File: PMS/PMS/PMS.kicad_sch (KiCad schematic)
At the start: 35 parts, among them IC1 TMCS1107A1BQDRQ1, J1 XT60PW-M, J2 XT60PW-F, J3 XT60PW-M, J4 XT60PW-F, J5 XT60PW-F, J6 Conn_01x03_Male, J7 Conn_01x02_Male, U1 ADC101C027CIMK, U2 ADC101C027CIMK, U4 REF195

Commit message: changed solder jumper footprint and added silk labels for XT60 connectors
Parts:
- JP1: footprint Jumper:SolderJumper-2_P1.3mm_Bridged2Bar_Pad1.0x1.5mm -> Jumper:SolderJumper-2_P1.3mm_Bridged2Bar_RoundedPad1.0x1.5mm
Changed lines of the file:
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@@
     (property "Reference" "JP1" (id 0) (at 88.9 58.0095 0))
     (property "Value" "Jumper_2_Bridged" (id 1) (at 88.9 60.7846 0))
-    (property "Footprint" "Jumper:SolderJumper-2_P1.3mm_Bridged2Bar_Pad1.0x1.5mm" (id 2) (at 88.9 62.611 0)
+    (property "Footprint" "Jumper:SolderJumper-2_P1.3mm_Bridged2Bar_RoundedPad1.0x1.5mm" (id 2) (at 88.9 62.611 0)
       (effects (font (size 1.27 1.27)) hide)
     )
@@
     )
     (path "/cf54f418-c583-4eda-be64-e2658e9d7854"
-      (reference "JP1") (unit 1) (value "Jumper_2_Bridged") (footprint "Jumper:SolderJumper-2_P1.3mm_Bridged2Bar_Pad1.0x1.5mm")
+      (reference "JP1") (unit 1) (value "Jumper_2_Bridged") (footprint "Jumper:SolderJumper-2_P1.3mm_Bridged2Bar_RoundedPad1.0x1.5mm")
     )
     (path "/45100c78-fff6-4f44-a47d-2aea8091517a"

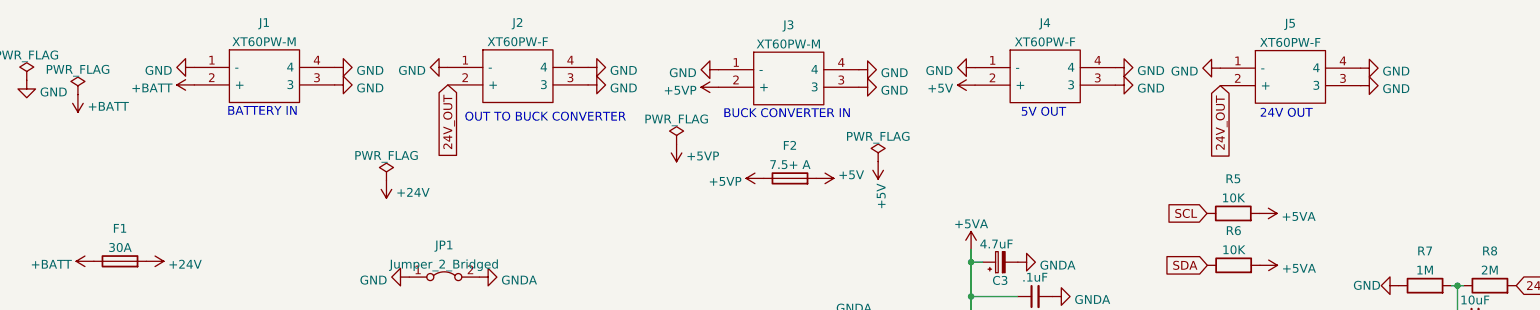
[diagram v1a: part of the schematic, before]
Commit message: changed to XT90s for 24V
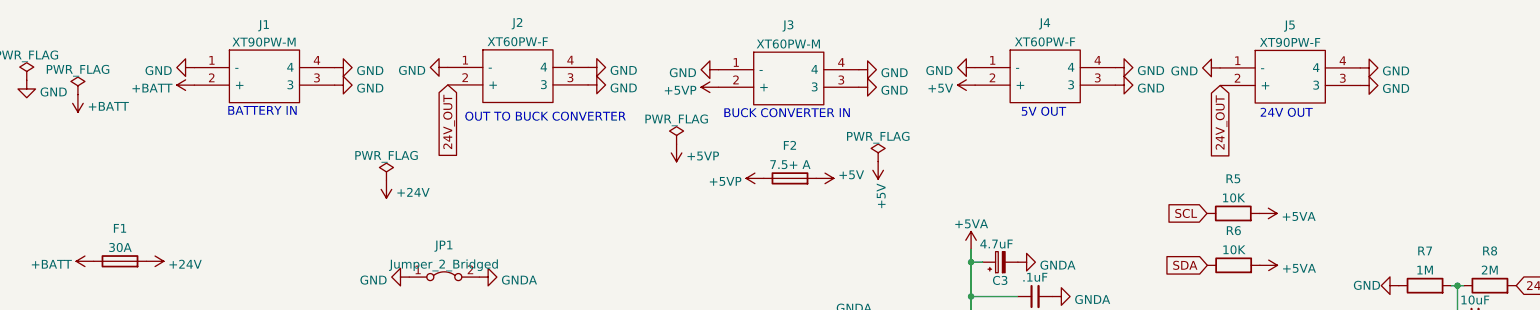
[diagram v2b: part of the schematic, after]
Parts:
- removed J1: XT60PW-M, LIB_XT60PW-M:XT60PWM, symbol XT60PW-M:XT60PW-M
- removed J5: XT60PW-F, LIB_XT60PW-F:XT60PWF, symbol XT60PW-F:XT60PW-F
- added J1: XT90PW-M, XT90PW-M:XT90PWM, symbol XT90PW-M:XT90PW-M
- added J5: XT90PW-F, XT90PW-F:XT90PW-F, symbol XT90PW-F:XT90PW-F
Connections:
- net +BATT: now also J1.2 (+)
- net 24V_OUT: now also J5.2 (+)
- net GND: now also J1.1 (-), J1.3, J1.4, J5.1 (-), J5.3, J5.4

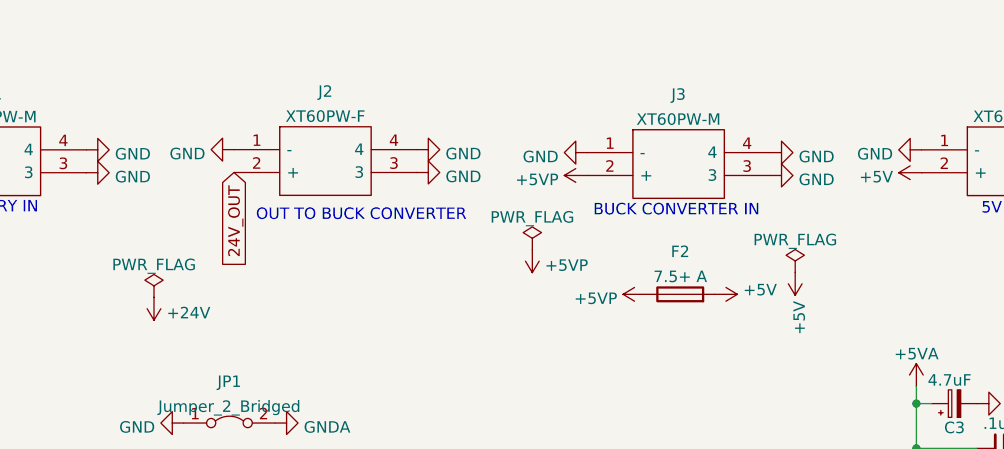
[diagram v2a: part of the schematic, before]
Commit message: Changed to barrier strip for connection to Mean-Well. Interconnects cannot be erroneously connected
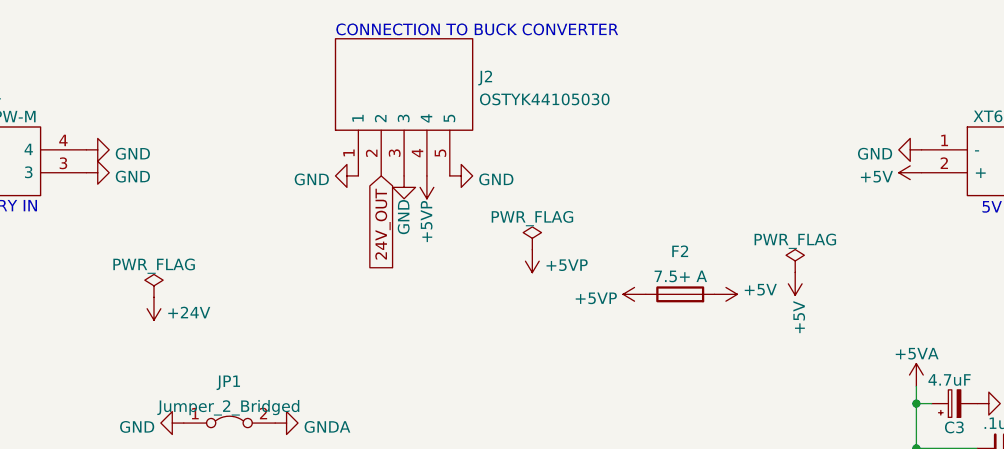
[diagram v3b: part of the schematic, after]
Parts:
- removed J2: XT60PW-F, LIB_XT60PW-F:XT60PWF, symbol XT60PW-F:XT60PW-F
- removed J3: XT60PW-M, LIB_XT60PW-M:XT60PWM, symbol XT60PW-M:XT60PW-M
- added J2: OSTYK44105030, LIB_OSTYK44105030:OSTYK44105030, symbol OSTYK44105030:OSTYK44105030
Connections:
- net +5VP: now also J2.4
- net 24V_OUT: now also J2.2
- net GND: now also J2.1, J2.3, J2.5
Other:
- note added: "CONNECTION TO BUCK CONVERTER"
- note removed: "BUCK CONVERTER IN"
- note removed: "OUT TO BUCK CONVERTER"

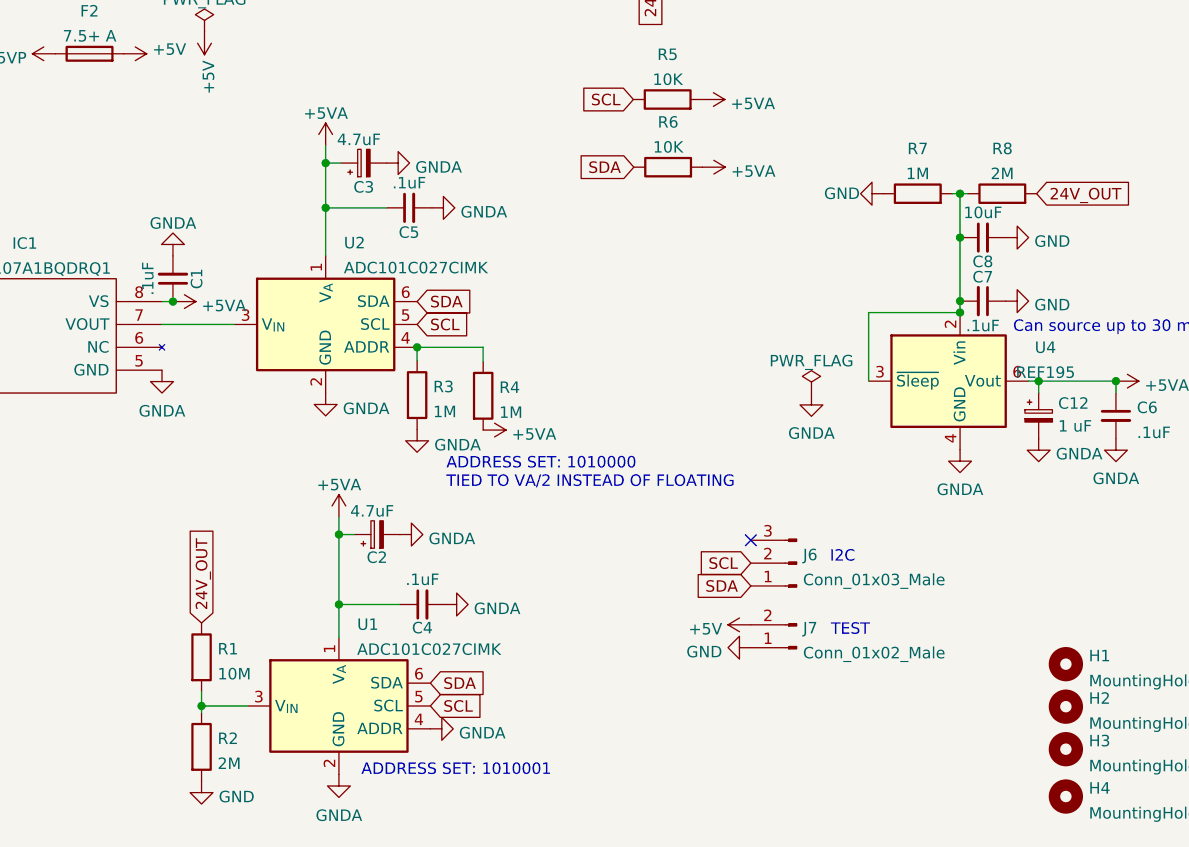
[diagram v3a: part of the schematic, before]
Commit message: updated PMS. Resistor values chosen for accurate current. ADC layouts altered to add via fence and reduce EMI. ADC input low-pass capacitors added.
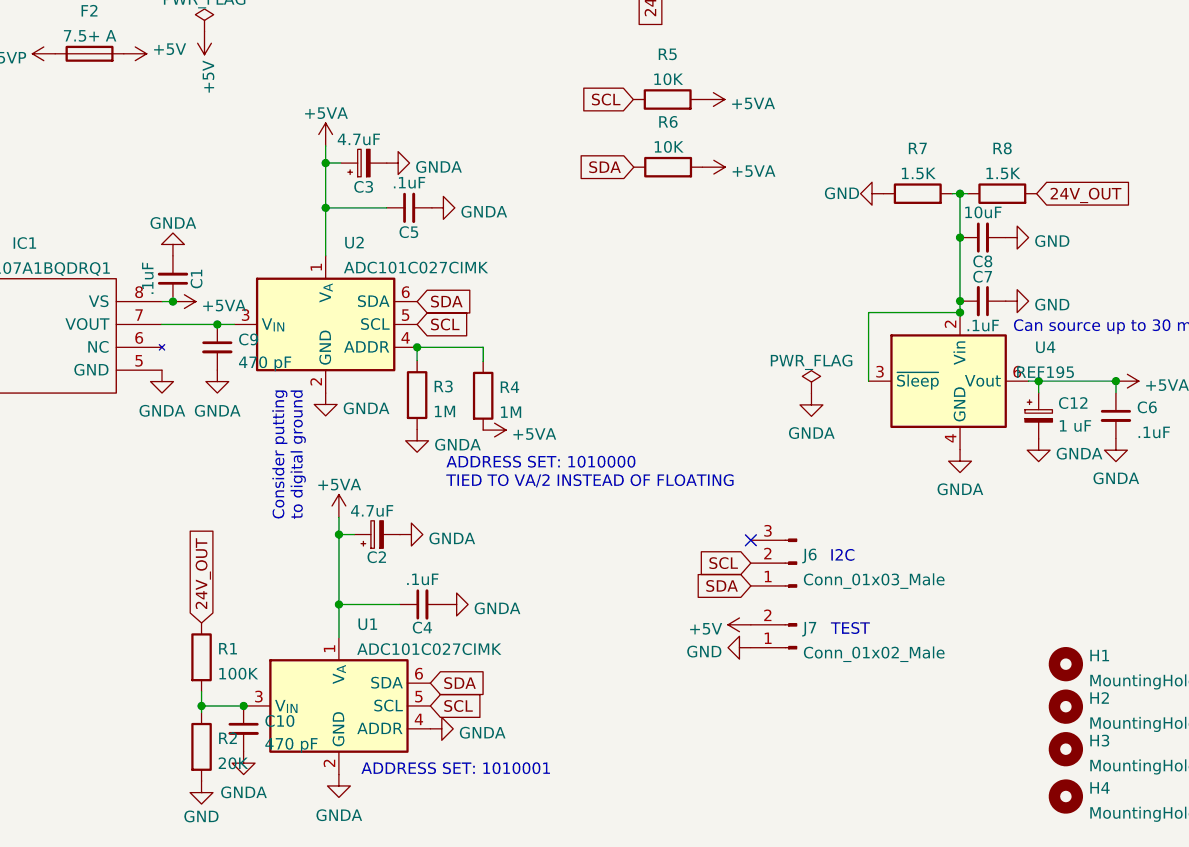
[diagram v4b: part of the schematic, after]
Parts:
- added C10, C9: 470 pF, Capacitor_SMD:C_0805_2012Metric_Pad1.18x1.45mm_HandSolder, symbol Device:C_Small
- C8: DigiKey Part Number (none) -> 399-C0805C106K4PAC7210CT-ND
- J2: DigiKey Part Number (none) -> ED2974-ND
- R1: value 10M -> 100K
- R2: value 2M -> 20K
- R7: value 1M -> 1.5K; Comments (none) -> Can also be 480
- R8: value 2M -> 1.5K; Comments (none) -> Can also be 240
- U4: DigiKey Part Number (none) -> REF195FSZ-REELCT-ND
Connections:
- net GNDA: now also C10.2, C9.2
- net at IC1.7 (VOUT), U2.3 (V_{IN}): now also C9.1
- net at R1.2, R2.1, U1.3 (V_{IN}): now also C10.1
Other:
- note added: "Consider putting to digital ground"

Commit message: minor changes
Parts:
- removed JP1: Jumper_2_Bridged, Jumper:SolderJumper-2_P1.3mm_Bridged2Bar_RoundedPad1.0x1.5mm, symbol Jumper:Jumper_2_Bridged
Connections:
- net GNDA is gone; now on net GND: C1.2, C10.2, C12.2, C2.2, C3.2, C4.2, C5.2, C6.2, C9.2, IC1.5 (GND), R3.2, U1.2 (GND), U1.4 (ADDR), U2.2 (GND), U4.4 (GND)
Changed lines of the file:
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@@
     (pin "6")
   )
-  (symbol (lib_id "power:GND") (at 83.82 62.611 270) (unit 1)
-    (in_bom yes) (on_board yes) (fields_autoplaced)
-    (property "Reference" "#PWR015" (id 0) (at 77.47 62.611 0)
-      (effects (font (size 1.27 1.27)) hide)
-    )
-    (property "Value" "GND" (id 1) (at 80.6451 63.09 90)
-      (effects (font (size 1.27 1.27)) (justify right))
-    )
-    (property "Footprint" "" (id 2) (at 83.82 62.611 0)
-      (effects (font (size 1.27 1.27)) hide)
-    )
-    (property "Datasheet" "" (id 3) (at 83.82 62.611 0)
+  (symbol (lib_id "power:GND") (at 93.98 62.611 270) (unit 1)
+    (in_bom yes) (on_board yes) (fields_autoplaced)
+    (property "Reference" "#PWR015" (id 0) (at 87.63 62.611 0)
+      (effects (font (size 1.27 1.27)) hide)
+    )
+    (property "Value" "GND" (id 1) (at 90.8051 63.09 90)
+      (effects (font (size 1.27 1.27)) (justify right))
+    )
+    (property "Footprint" "" (id 2) (at 93.98 62.611 0)
+      (effects (font (size 1.27 1.27)) hide)
+    )
+    (property "Datasheet" "" (id 3) (at 93.98 62.611 0)
       (effects (font (size 1.27 1.27)) hide)
     )
@@
     )
   )
-  (symbol (lib_id "Jumper:Jumper_2_Bridged") (at 88.9 62.611 0) (unit 1)
-    (in_bom yes) (on_board yes) (fields_autoplaced)
-    (property "Reference" "JP1" (id 0) (at 88.9 58.0095 0))
-    (property "Value" "Jumper_2_Bridged" (id 1) (at 88.9 60.7846 0))
-    (property "Footprint" "Jumper:SolderJumper-2_P1.3mm_Bridged2Bar_RoundedPad1.0x1.5mm" (id 2) (at 88.9 62.611 0)
-      (effects (font (size 1.27 1.27)) hide)
-    )
-    (property "Datasheet" "~" (id 3) (at 88.9 62.611 0)
-      (effects (font (size 1.27 1.27)) hide)
-    )
-    (pin "1")
-    (pin "2")
-  )
   (symbol (lib_id "power:+5V") (at 142.7988 48.3108 270) (unit 1)
     (in_bom yes) (on_board yes)
@@
       (reference "J7") (unit 1) (value "Conn_01x02_Male") (footprint "Connector_JST:JST_XH_B2B-XH-AM_1x02_P2.50mm_Vertical")
     )
-    (path "/cf54f418-c583-4eda-be64-e2658e9d7854"
-      (reference "JP1") (unit 1) (value "Jumper_2_Bridged") (footprint "Jumper:SolderJumper-2_P1.3mm_Bridged2Bar_RoundedPad1.0x1.5mm")
-    )
     (path "/45100c78-fff6-4f44-a47d-2aea8091517a"

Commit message: increased distance between planes. Improved top GND plane for analog portion of board. simplified some geometries. VIAS.
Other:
- note added: "ADC for battery voltage."
- note added: "ADC for current sensor."
- note added: "Precision reference. Provides 5V DC power for sensors on board."
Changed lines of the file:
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@@
+    (effects (font (size 1.27 1.27)) (justify left bottom))
+  )
+  (text "ADC for current \nsensor." (at 186.1312 79.2734 0)
     (effects (font (size 1.27 1.27)) (justify left bottom))
   )
@@
   )
   (text "BATTERY IN" (at 57.4294 39.497 0)
+    (effects (font (size 1.27 1.27)) (justify left bottom))
+  )
+  (text "ADC for battery \nvoltage." (at 188.2902 122.3264 0)
     (effects (font (size 1.27 1.27)) (justify left bottom))
   )
@@
     (effects (font (size 1.27 1.27)) (justify left bottom))
   )
+  (text "Precision reference.\nProvides 5V DC power for \nsensors on board."
+    (at 257.1242 72.9234 0)
+    (effects (font (size 1.27 1.27)) (justify left bottom))
+  )
